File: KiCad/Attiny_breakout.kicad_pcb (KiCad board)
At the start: 2 copper layers, 40.6 x 68.2 mm, 63 parts, among them J1 ICSP, J2 PowerConn, J3 Conn_01x07_Female, J4 Conn_01x07_Female, J5 12V_conn, J6 HVP_EN_conn, J7 USB_C_Receptacle_USB2.0, Q1 AO3401A, Q2 BC847C, SW1 SW_DIP_x02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

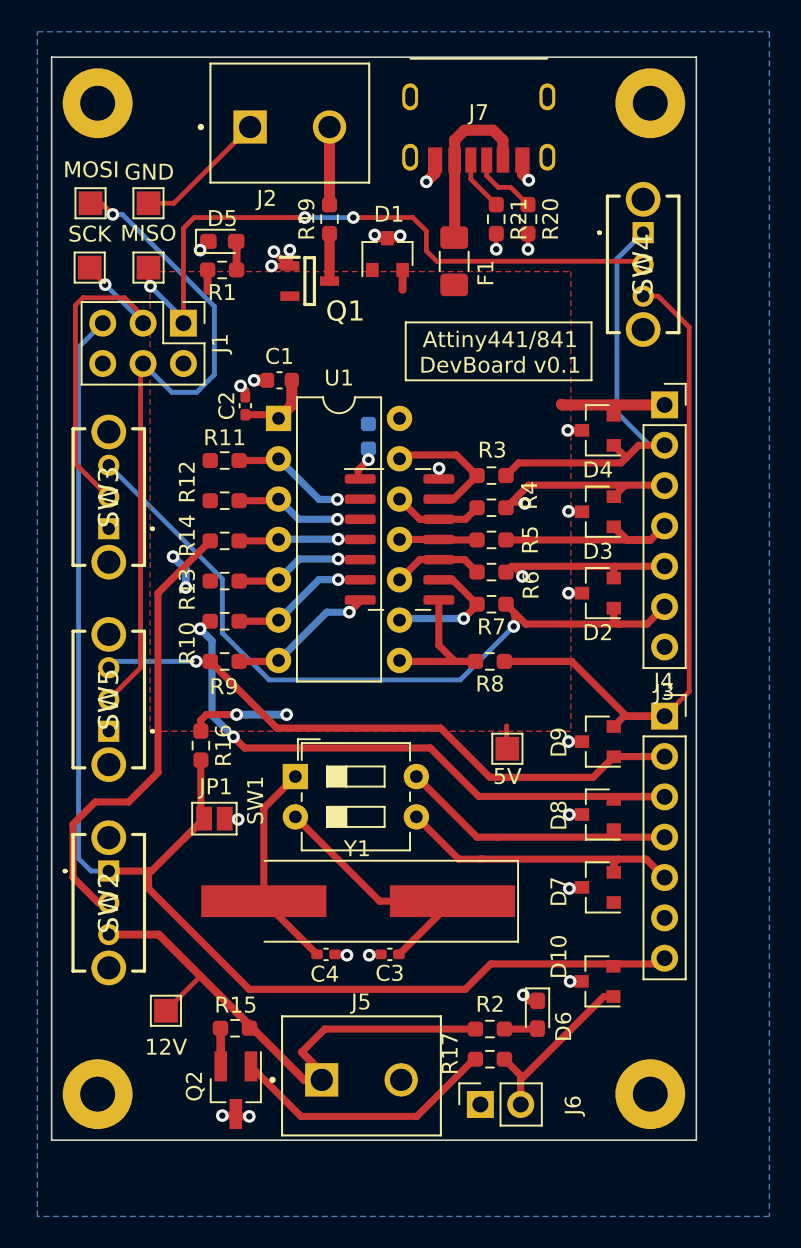
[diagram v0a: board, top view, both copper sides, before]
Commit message: Final version of PCB. Removed unnecessary SPI connections.
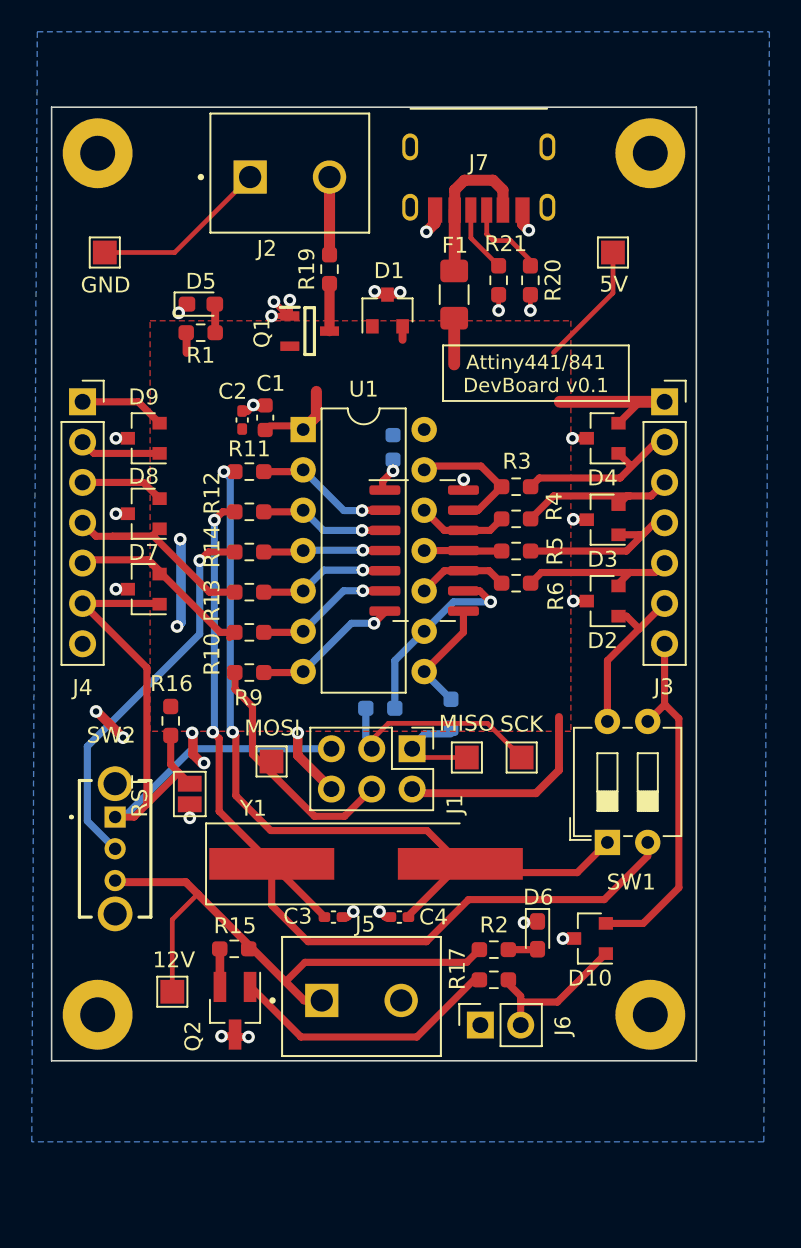
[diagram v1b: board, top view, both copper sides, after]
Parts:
- removed SW3, SW4, SW5: SW_SPDT, Attiny_breakout:SS12D07L4B
- added G***: LOGO, NadSilk:brain_logo_smol, B.Cu at (232.3, 55.7)
- R7, R8: moved to B.Cu
- moved J4 41.7 mm to (222.8, 58.6)
- moved TP5 41.1 mm to (250.5, 81.0)
- moved TP3 37.0 mm to (234.8, 81.2)
- moved TP4 36.8 mm to (247.1, 81.0)
- moved D9 34.4 mm to (226.7, 60.9)
- moved D8 34.3 mm to (226.7, 65.7)
- moved D7 34.2 mm to (226.7, 70.4)
- moved TP1 31.9 mm to (256.2, 49.2)
- moved J1 30.4 mm to (243.6, 80.5)
- moved SW1 20.1 mm to (255.9, 86.3), turned to 90 degrees
- moved R7 9.59 mm to (241.6, 77.9), turned to 0 degrees
- moved C4 5.18 mm to (242.8, 91.0), turned to 180 degrees
- moved R17 5.01 mm to (248.8, 95.0)
- moved R2 5.01 mm to (248.8, 93.1)
- moved Q2 5.00 mm to (232.4, 97.0)
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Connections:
- net MISO1_A0 renamed A0
- net MOSI1_A1 renamed A1
- net SCK1_A3 renamed A3
- D10 pad 2: RST -> Net-(D10-Pad2)
- D2 pad 1: SCK2_A4 -> Net-(D2-Pad1)
- D7 pad 1: B2 -> RST
- D7 pad 2: Net-(D7-Pad2) -> A7
- D8 pad 1: Net-(D8-Pad1) -> B2
- D8 pad 2: A7 -> Net-(D8-Pad2)
- D9 pad 1: MOSI2_A6 -> Net-(D9-Pad1)
- D9 pad 2: MISO2_A5 -> Net-(D9-Pad2)
- J3 pad 6: SCK2_A4 -> Net-(D2-Pad1)
- J3 pad 7: GND -> Net-(D10-Pad2)
- J4 pad 1: MISO2_A5 -> Net-(D9-Pad2)
- J4 pad 2: MOSI2_A6 -> Net-(D9-Pad1)
- J4 pad 3: A7 -> Net-(D8-Pad2)
- J4 pad 4: Net-(D8-Pad1) -> B2
- J4 pad 5: Net-(D7-Pad2) -> A7
- J4 pad 6: B2 -> RST
- J4 pad 7: RST -> GND
- R7 pad 1: SCK2_A4 -> SCK
- R8 pad 1: MISO2_A5 -> MISO
- R9 pad 1: MOSI2_A6 -> MOSI
- SW1 pad 3: Net-(D7-Pad2) -> Net-(D10-Pad2)
- SW1 pad 4: Net-(D8-Pad1) -> Net-(D2-Pad1)
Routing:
- net SCK2_A4: track 47.4 -> 0.00 mm, vias 1 -> 0
- net MISO2_A5: track 43.8 -> 0.00 mm
- net RST: track 86.4 -> 43.3 mm
- net B1_XTAL2: track 16.8 -> 59.8 mm, vias 0 -> 2
- net B0_XTAL1: track 13.4 -> 52.4 mm, vias 0 -> 2
- net MOSI2_A6: track 38.7 -> 0.00 mm, vias 1 -> 0
- net MISO: track 41.6 -> 6.45 mm, vias 3 -> 0
- net A7: track 40.5 -> 13.2 mm, vias 2 -> 0
- net MOSI: track 43.3 -> 16.4 mm, vias 1 -> 0
- net Net-(D10-Pad2): track 0.00 -> 22.8 mm
- net VCC: track 27.2 -> 47.8 mm, vias 5 -> 3
- net Net-(D7-Pad2): track 18.3 -> 0.00 mm
- net Net-(D8-Pad1): track 17.8 -> 0.00 mm
- net A0: track 27.8 -> 10.7 mm
- net B2: track 0.00 -> 14.6 mm
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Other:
- board size 40.6 x 68.2 mm -> 40.6 x 60 mm
- board text added: "A0"
- board text added: "A1"
- board text added: "A2"
- board text added: "A3"
- board text added: "A7"
- board text added: "B0"
- board text added: "B1"
- board text added: "B2"
- board text added: "GND"
- board text added: "HVSP"
- board text added: "HVSP 12V"
- board text added: "HVSP SIG"
- board text added: "ICSP"
- board text added: "MISO"
- board text added: "MOSI"
- board text added: "RST"
- board text added: "SCK"
- board text added: "Switch off if using Crystal"
- board text added: "Switch to HVSP when resetting fuses"
- board text added: "USB 5V"
- board text added: "VCC"
- board text added: "VCC input"
